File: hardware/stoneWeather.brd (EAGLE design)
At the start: 63.2 x 30.5 mm, 27 parts, among them IC1 ATMEGA328, IC2 AMS1117

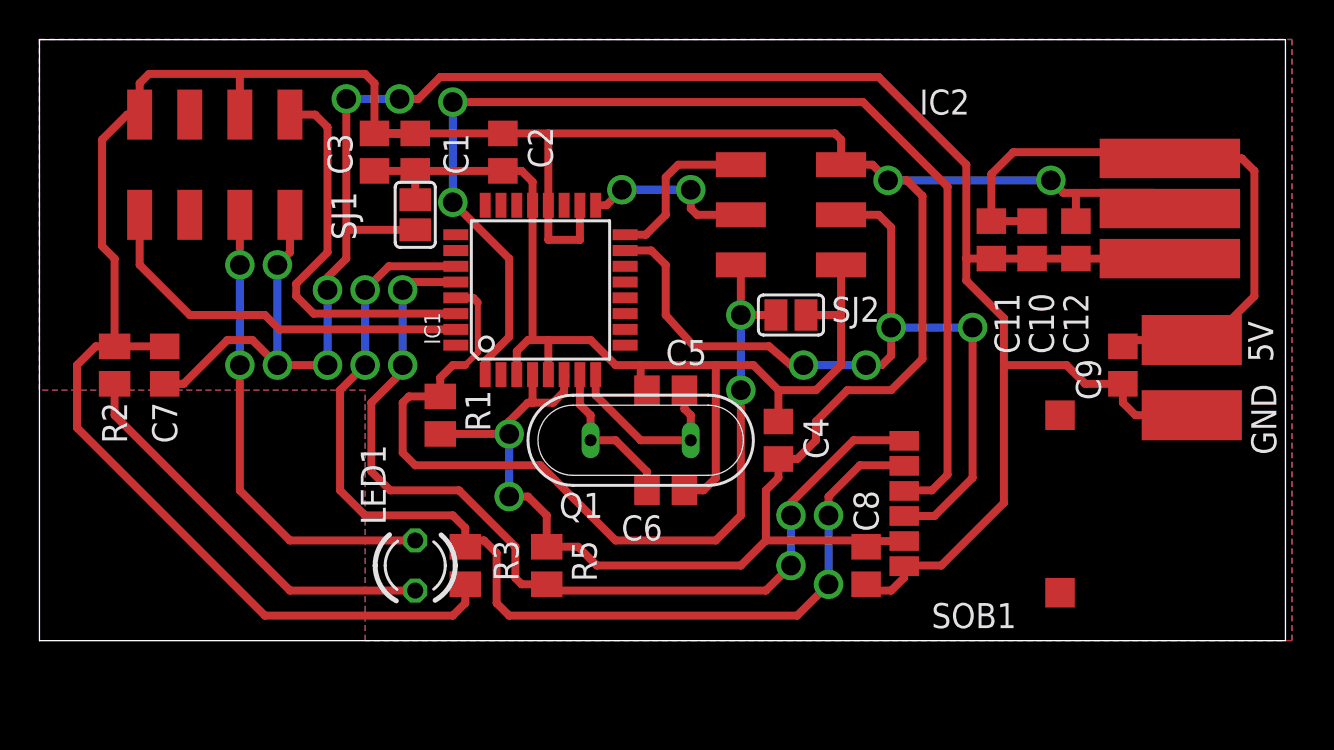
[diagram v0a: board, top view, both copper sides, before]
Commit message: Added GY21-HTU21 breakout board header to the board Updated README.md
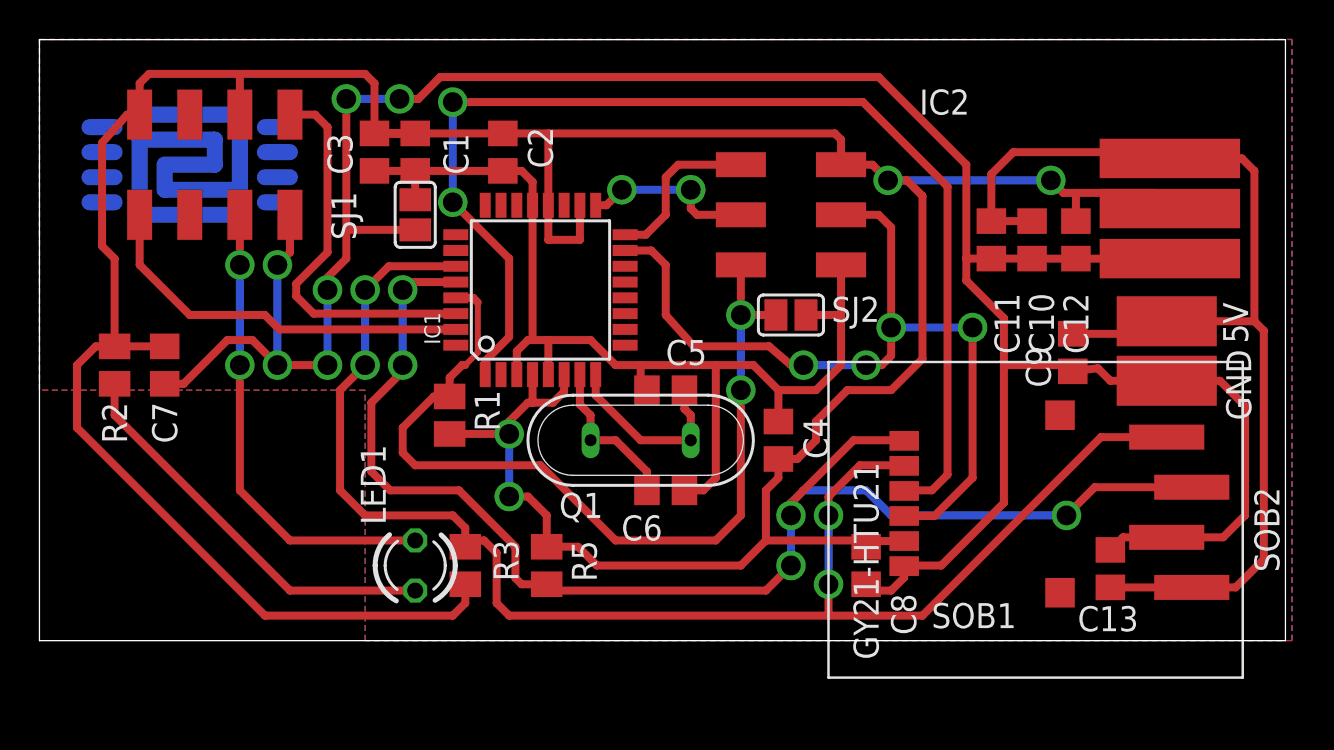
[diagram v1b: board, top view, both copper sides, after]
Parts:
- added C13: (no value), rcl:C0805
- added SOB2: (no value), stoneTronics:GY21-HTU21
- moved C9 2.62 mm to (52.4, 14.6)
- moved GND 2.16 mm to (57.1, 13.2)
- moved 5V 1.59 mm to (57.1, 16.2)
- moved R1 0.48 mm to (20.8, 11.4)
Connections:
- removed net N$2: 5V.P$1, C10.1, C11.1, C9.1, IC2.IN
- new net +5V: 5V.P$1, C10.1, C11.1, C13.1, C9.1, IC2.IN, SOB2.P$4
- net GND: now also C13.2, SOB2.P$3
- net SCL: now also SOB2.P$2
- net SDA: now also SOB2.P$1
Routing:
- net +5V: track 0.00 -> 61.4 mm
- net N$2: track 33.1 -> 0.00 mm
- net N$5: track 0.00 -> 33.0 mm
- net SCL: track 48.4 -> 70.7 mm, vias 4 -> 5
- net SDA: track 55.0 -> 76.8 mm
- net GND: track 117.4 -> 132.7 mm
- net N$9: track 0.00 -> 1.27 mm
- net N$8: track 0.00 -> 1.27 mm
- net N$7: track 0.00 -> 1.27 mm
- net N$6: track 0.00 -> 1.27 mm
- net N$13: track 0.00 -> 1.27 mm
- net N$12: track 0.00 -> 1.27 mm
- net N$11: track 0.00 -> 1.27 mm
- net N$10: track 0.00 -> 1.27 mm
- net RST: track 45.7 -> 45.0 mm
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- added copper zone on layer 1, net +3V3
- removed copper zone on layer 1, net GND
